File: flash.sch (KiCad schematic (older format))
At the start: 3 parts, among them J2 JTAG, U1 LFE5U-12F-8BG256C, U2 W25Q128JVSIQ

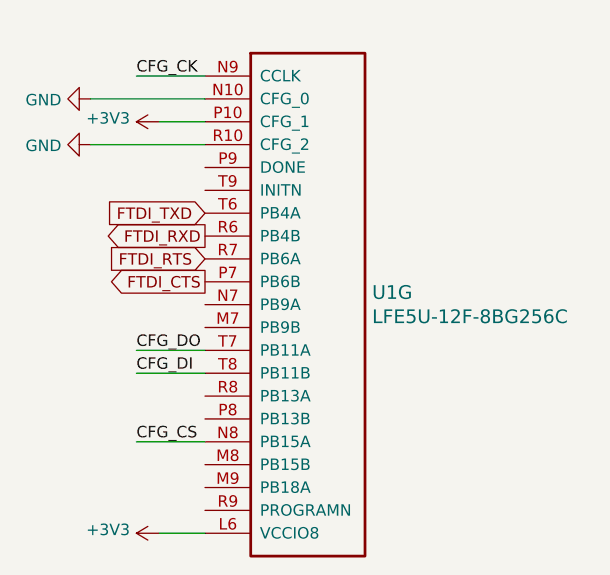
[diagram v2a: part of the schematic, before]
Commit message: add hdmi output
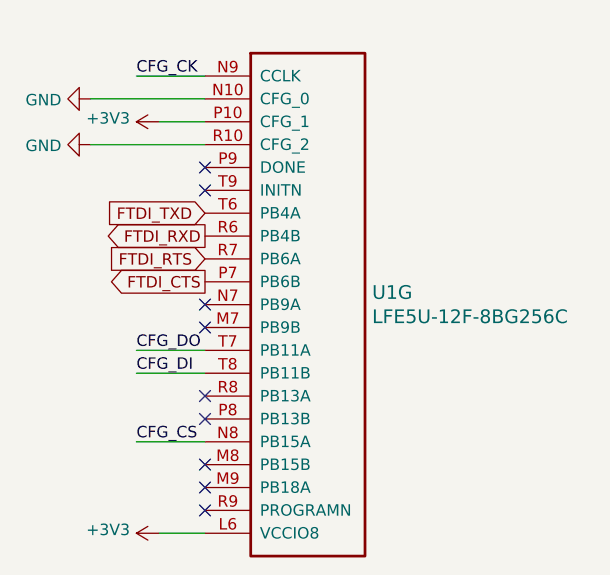
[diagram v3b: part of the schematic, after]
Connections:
- no-connect marks 3 -> 12
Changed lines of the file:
@@
 $Descr A4 11693 8268
 encoding utf-8
-Sheet 4 7
+Sheet 4 8
 Title ""
 Date ""
@@
 Text GLabel 2400 3500 0    50   Output ~ 0
 FTDI_CTS
+NoConn ~ 2400 3000
+NoConn ~ 2400 3100
+NoConn ~ 2400 3600
+NoConn ~ 2400 3700
+NoConn ~ 2400 4000
+NoConn ~ 2400 4100
+NoConn ~ 2400 4300
+NoConn ~ 2400 4400
+NoConn ~ 2400 4500
 $EndSCHEMATC
